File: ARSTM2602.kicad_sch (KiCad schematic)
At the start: 36 parts, among them J1 Conn_01x02_Socket, J11 Conn_01x02_Socket, J12 Conn_01x02_Socket, J13 Conn_01x02_Socket, J8 Conn_01x02_Socket, J9 Conn_ST_STDC14, SW2 SW_SPDT, SW3 SW_Push, SW5 SW_Wuerth_450301014042, SW6 SW_Wuerth_450301014042, U2 TCAN3414DRBR, U3 TCAN3414DRBR, U4 STM32H523CCTx, U5 BD33FC0FP

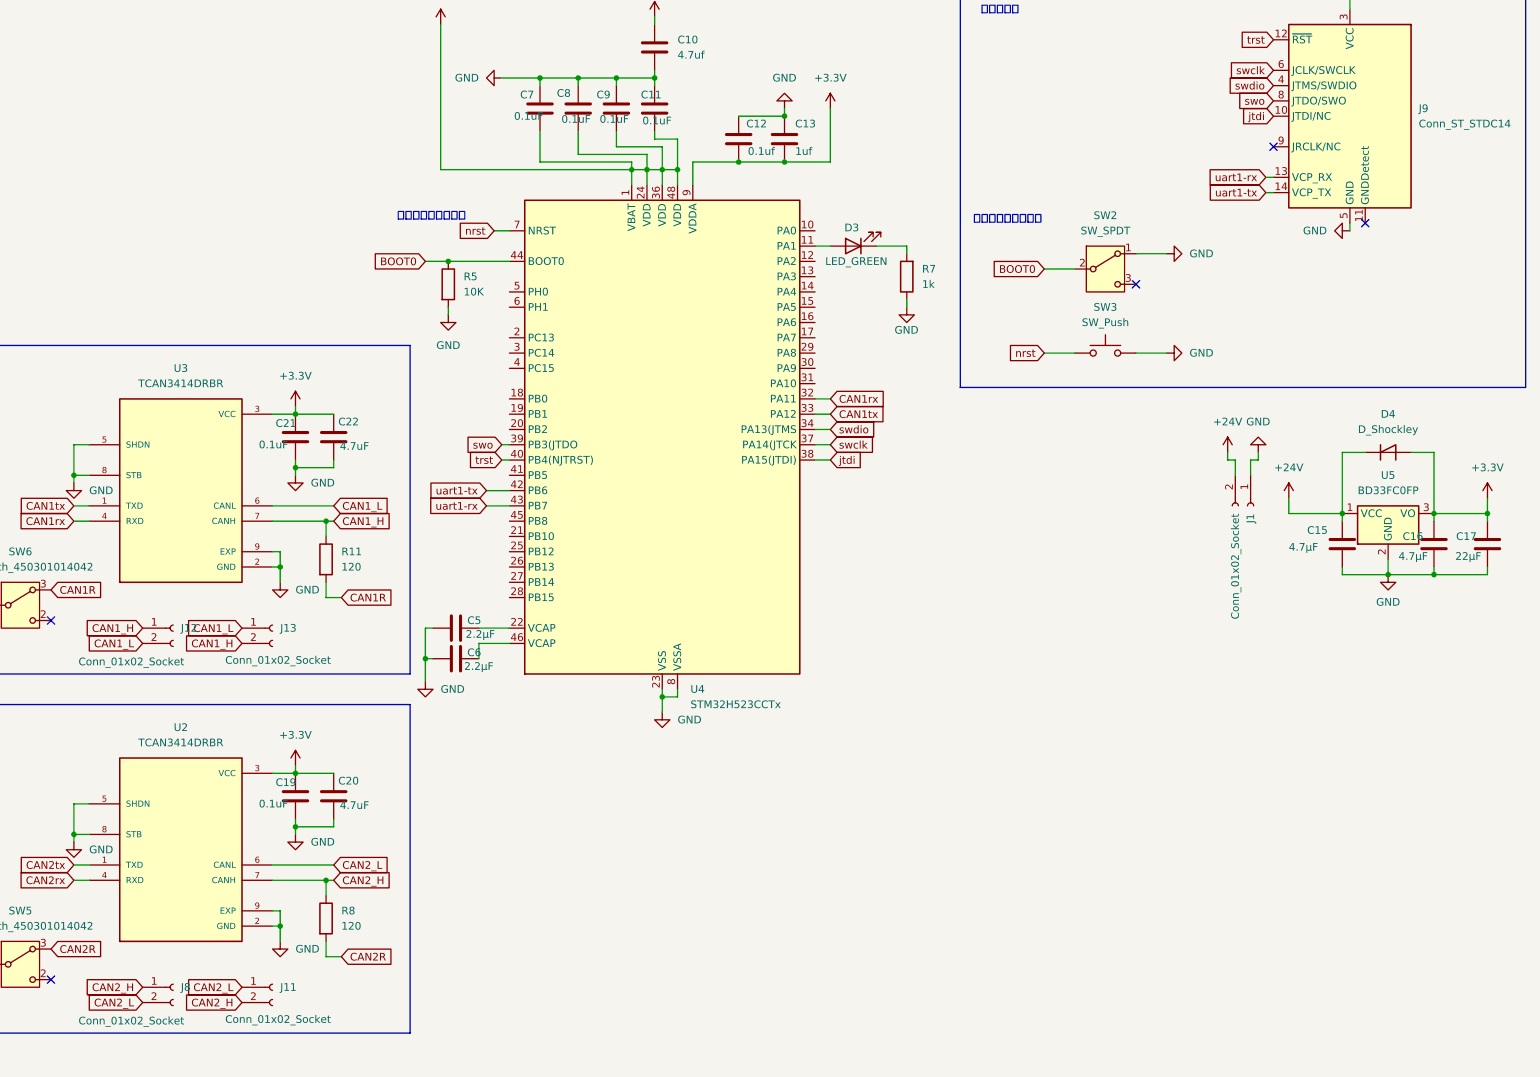
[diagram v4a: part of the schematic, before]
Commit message: サブマイコンx2を配置
ESPとラズパイを置いた
ラズパイはまだ途中
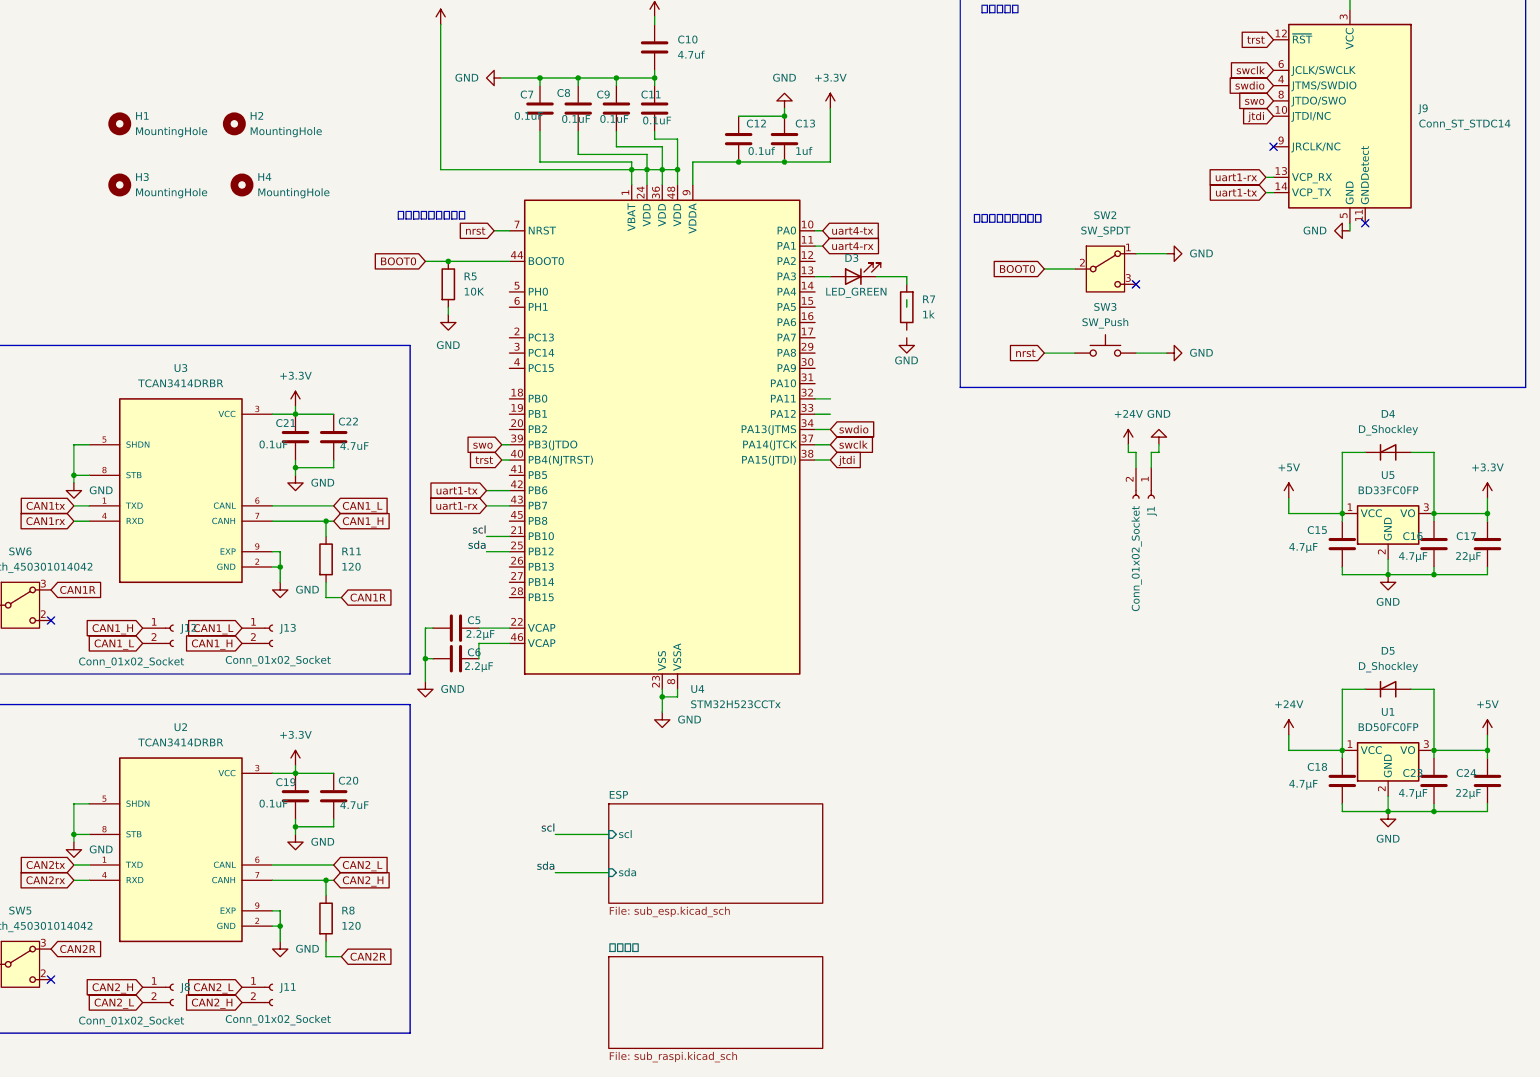
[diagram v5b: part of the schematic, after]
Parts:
- added C18, C23: 4.7μF, Capacitor_SMD:C_0805_2012Metric_Pad1.18x1.45mm_HandSolder, symbol Device:C
- added C24: 22μF, Capacitor_SMD:C_0805_2012Metric_Pad1.18x1.45mm_HandSolder, symbol Device:C
- added D5: D_Shockley, Diode_SMD:D_SOD-323_HandSoldering, symbol Device:D_Shockley
- added H1, H2, H3, H4: MountingHole, MountingHole:MountingHole_3.2mm_M3, symbol Mechanical:MountingHole
- added U1: BD50FC0FP, Package_TO_SOT_SMD:TO-252-2, symbol Regulator_Linear:BD50FC0FP
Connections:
- net +24V: now also C18.1, D5.1 (K), U1.1 (VCC); no longer C15.1, D4.1 (K), U5.1 (VCC)
- net CAN1rx: no longer U4.32 (PA11)
- net CAN1tx: no longer U4.33 (PA12)
- net GND: now also C18.2, C23.2, C24.2, U1.2 (GND); no longer R7.1
- net uart4-tx: now reaches U4.10 (PA0)
- net at D3.2 (A): now also U4.13 (PA3); no longer U4.11 (PA1)
- net scl: now reaches U4.21 (PB10)
- net sda: now reaches U4.25 (PB12)
- new net +5V: C15.1, C23.1, C24.1, D4.1 (K), D5.2 (A), U1.3 (VO), U5.1 (VCC)
- new net uart4-rx: U4.11 (PA1)
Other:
- added sheet ESP (sub_esp.kicad_sch)
- added sheet ラズパイ (sub_raspi.kicad_sch)
- moved on the sheet: J1

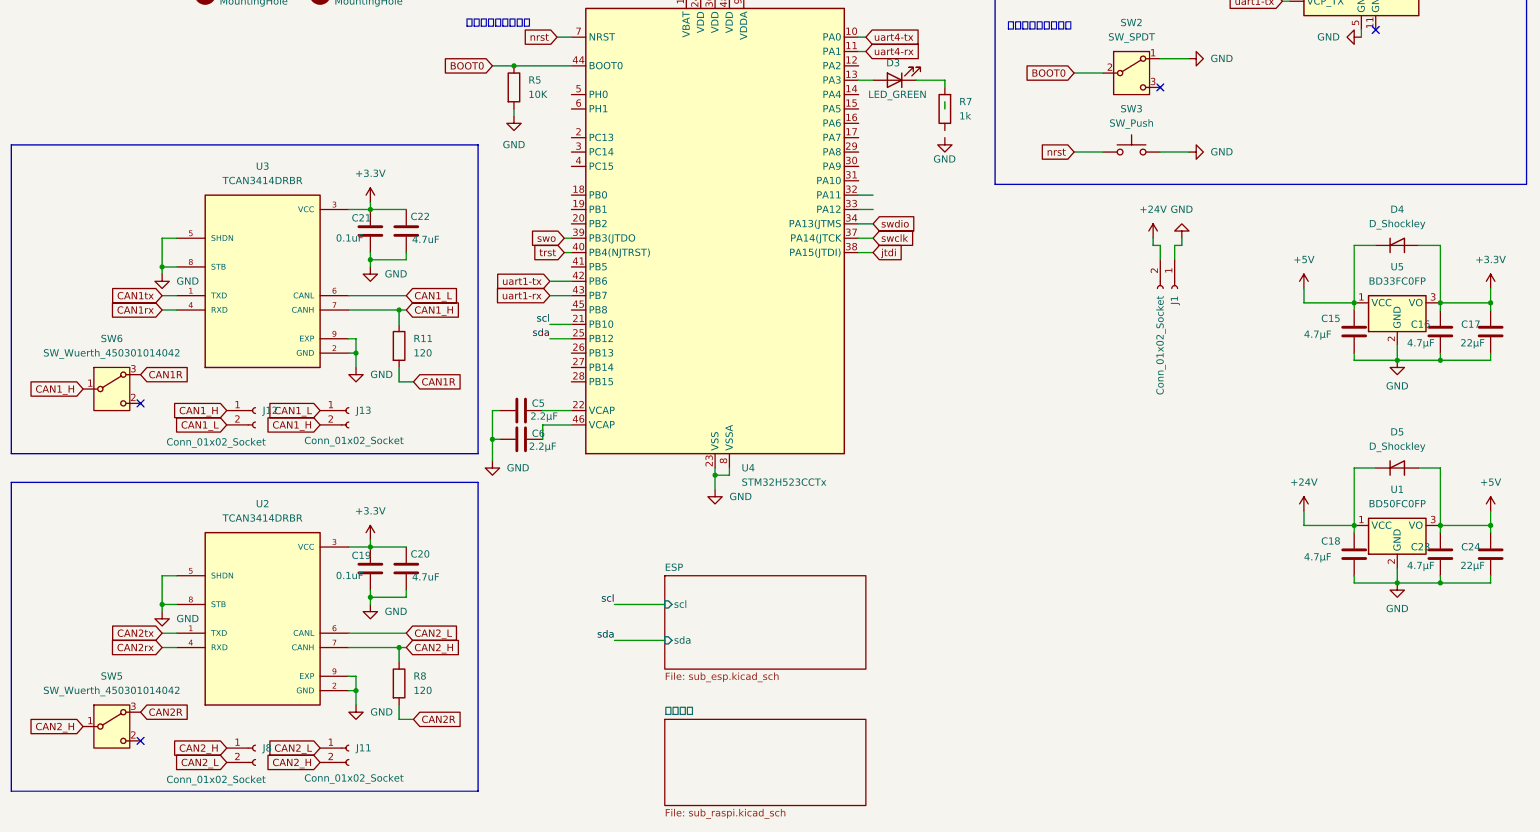
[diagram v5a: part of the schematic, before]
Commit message: 一部回路図変更と部品配置
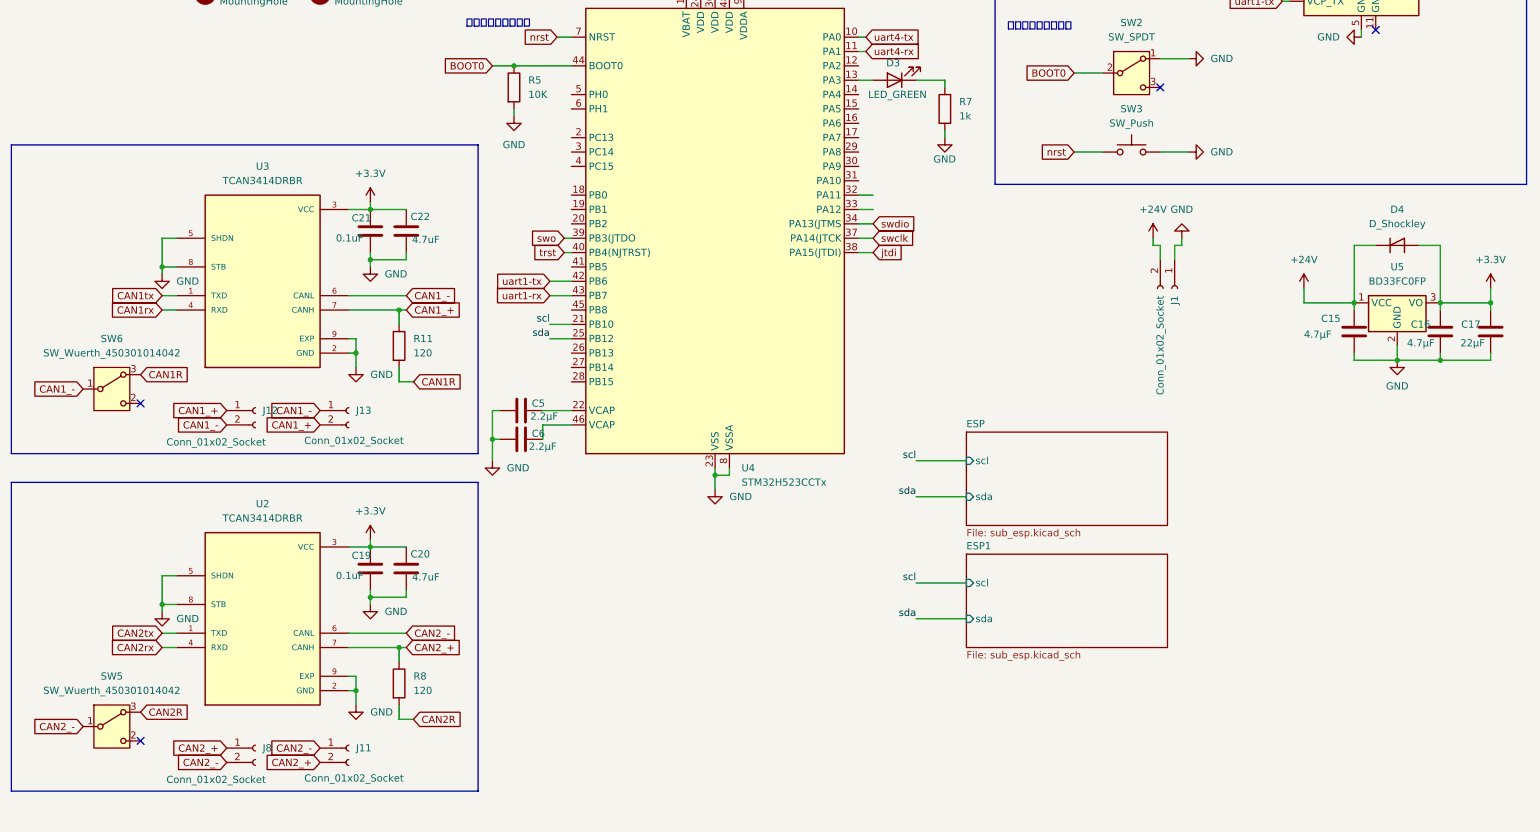
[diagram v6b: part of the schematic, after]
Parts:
- removed C18, C23: 4.7μF, Capacitor_SMD:C_0805_2012Metric_Pad1.18x1.45mm_HandSolder, symbol Device:C
- removed C24: 22μF, Capacitor_SMD:C_0805_2012Metric_Pad1.18x1.45mm_HandSolder, symbol Device:C
- removed D5: D_Shockley, Diode_SMD:D_SOD-323_HandSoldering, symbol Device:D_Shockley
- removed U1: BD50FC0FP, Package_TO_SOT_SMD:TO-252-2, symbol Regulator_Linear:BD50FC0FP
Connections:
- net +5V is gone; now on net +24V: C15.1, D4.1 (K), U5.1 (VCC)
- net GND: now also R7.1
- net CAN1_H renamed CAN1_+
- net CAN1_+: no longer SW6.1 (B)
- net CAN1_L renamed CAN1_-
- net CAN1_-: now also SW6.1 (B)
- net CAN2_H renamed CAN2_+
- net CAN2_+: no longer SW5.1 (B)
- net CAN2_L renamed CAN2_-
- net CAN2_-: now also SW5.1 (B)
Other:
- removed sheet ラズパイ
- added sheet ESP1 (sub_esp.kicad_sch)

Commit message: 電磁弁用回路の増設
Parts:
- removed SW5, SW6: SW_Wuerth_450301014042, Button_Switch_THT:SW_Slide-03_Wuerth-WS-SLTV_10x2.5x6.4_P2.54mm, symbol Switch:SW_Wuerth_450301014042
- added C14, C18, C23, C29, C32: 0.1uF, Capacitor_SMD:C_0603_1608Metric_Pad1.08x0.95mm_HandSolder, symbol Device:C
- added C24: 4.7uf, Capacitor_SMD:C_0805_2012Metric_Pad1.18x1.45mm_HandSolder, symbol Device:C
- added C30: 0.1uf, Capacitor_SMD:C_0603_1608Metric_Pad1.08x0.95mm_HandSolder, symbol Device:C
- added C31, C33: 1uf, Capacitor_SMD:C_0603_1608Metric_Pad1.08x0.95mm_HandSolder, symbol Device:C
- added D1, D2, D5: D, symbol Device:D
- added J10, J14, J15: Conn_01x02_Socket, Connector_JST:JST_XH_S2B-XH-A-1_1x02_P2.50mm_Horizontal, symbol Connector:Conn_01x02_Socket
- added J2: Conn_01x02_Socket, Connector_AMASS:AMASS_XT30PW-M_1x02_P2.50mm_Horizontal, symbol Connector:Conn_01x02_Socket
- added Q2, Q5, Q6: Q_NMOS_GSD, Package_TO_SOT_SMD:SOT-23_Handsoldering, symbol Transistor_FET:Q_NMOS_GSD
- added R15, R17, R19: 330, Resistor_SMD:R_0603_1608Metric_Pad0.98x0.95mm_HandSolder, symbol Device:R
- added R16, R18, R20, R21, R22, R23: 10k, Resistor_SMD:R_0603_1608Metric_Pad0.98x0.95mm_HandSolder, symbol Device:R_Small
- added SW10: SW_DPDT_x2, symbol Switch:SW_DPDT_x2
- added SW9: SW_DPDT_x2, Button_Switch_THT:SW_Slide-03_Wuerth-WS-SLTV_10x2.5x6.4_P2.54mm, symbol Switch:SW_DPDT_x2
- added U1: STM32G431RBTx, Package_QFP:LQFP-64_10x10mm_P0.5mm, symbol MCU_ST_STM32G4:STM32G431RBTx
- added U12, U8, U9: TLP785, Package_DIP:DIP-4_W7.62mm, symbol Isolator:TLP785
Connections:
- net +24V: now also D1.1 (K), D2.1 (K), D5.1 (K), J10.1 (Pin_1), J14.1 (Pin_1), J15.1 (Pin_1), J2.1 (Pin_1), U12.4, U8.4, U9.4
- net +3.3V: now also C14.1, C18.1, C23.1, C24.1, C29.1, C30.2, C31.2, C32.1, C33.2, U1.1 (VBAT), U1.16 (VDD), U1.28 (VREF+), U1.29 (VDDA), U1.32 (VDD), U1.48 (VDD), U1.64 (VDD)
- net CAN1R: now also SW10.1 (A)
- net CAN1_-: now also SW10.2 (B)
- net CAN1rx: now also U4.32 (PA11)
- net CAN1tx: now also U4.33 (PA12)
- net CAN2R: now also SW9.1 (A)
- net CAN2_-: now also SW9.2 (B)
- net CAN2rx: now also U4.25 (PB12)
- net CAN2tx: now also U4.26 (PB13)
- net GND: now also C14.2, C18.2, C23.2, C24.2, C29.2, C30.1, C31.1, C32.2, C33.1, U1.15 (VSS), U1.27 (VSSA), U1.31 (VSS), U1.47 (VSS), U1.63 (VSS), U12.2, U8.2, U9.2
- net scl: no longer U4.21 (PB10)
- net sda: no longer U4.25 (PB12)
- new net: D5.2 (A), J10.2 (Pin_2), Q2.3 (D)
- new net: R16.1, U8.3
- new net: Q2.1 (G), R16.2, R22.1
- new net: Q5.1 (G), R18.2, R21.1
- new net: D2.2 (A), J14.2 (Pin_2), Q5.3 (D)
- new net: R17.1, U9.1
- new net: R18.1, U9.3
- new net: D1.2 (A), J15.2 (Pin_2), Q6.3 (D)
- new net: R20.1, U12.3
- new net: Q6.1 (G), R20.2, R23.1
- new net: R15.1, U8.1
- new net: R19.1, U12.1
- new net GND1: J2.2 (Pin_2), Q2.2 (S), Q5.2 (S), Q6.2 (S), R21.2, R22.2, R23.2
- new net Si_1: R15.2
- new net Si_2: R17.2
- new net Si_3: R19.2
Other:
- moved on the sheet: C10, C11, C12, C13, C19, C20, C21, C22, C5, C6, C7, C8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

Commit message: 完成(電磁弁制御,モーター出力追加済み)
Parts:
- removed C10: 4.7uf, Capacitor_SMD:C_0805_2012Metric_Pad1.18x1.45mm_HandSolder, symbol Device:C
- removed C11, C19, C21, C7, C8, C9: 0.1uF, Capacitor_SMD:C_0603_1608Metric_Pad1.08x0.95mm_HandSolder, symbol Device:C
- removed C12: 0.1uf, Capacitor_SMD:C_0603_1608Metric_Pad1.08x0.95mm_HandSolder, symbol Device:C
- removed C13: 1uf, Capacitor_SMD:C_0603_1608Metric_Pad1.08x0.95mm_HandSolder, symbol Device:C
- removed C20, C22: 4.7uF, Capacitor_SMD:C_0603_1608Metric_Pad1.08x0.95mm_HandSolder, symbol Device:C
- removed C5, C6: 2.2μF, Capacitor_SMD:C_0603_1608Metric_Pad1.08x0.95mm_HandSolder, symbol Device:C
- removed D1, D2, D5: D, symbol Device:D
- removed D3: LED_GREEN, Capacitor_SMD:C_0603_1608Metric_Pad1.08x0.95mm_HandSolder, symbol Device:LED
- removed J10, J11, J12, J13, J14, J15, J8: Conn_01x02_Socket, Connector_JST:JST_XH_S2B-XH-A-1_1x02_P2.50mm_Horizontal, symbol Connector:Conn_01x02_Socket
- removed Q2, Q5, Q6: Q_NMOS_GSD, Package_TO_SOT_SMD:SOT-23_Handsoldering, symbol Transistor_FET:Q_NMOS_GSD
- removed R11, R8: 120, Resistor_SMD:R_0603_1608Metric_Pad0.98x0.95mm_HandSolder, symbol Device:R
- removed R15, R17, R19: 330, Resistor_SMD:R_0603_1608Metric_Pad0.98x0.95mm_HandSolder, symbol Device:R
- removed R16, R18, R20, R21, R22, R23: 10k, Resistor_SMD:R_0603_1608Metric_Pad0.98x0.95mm_HandSolder, symbol Device:R_Small
- removed R5: 10K, Resistor_SMD:R_0603_1608Metric_Pad0.98x0.95mm_HandSolder, symbol Device:R
- removed R7: 1k, Resistor_SMD:R_0603_1608Metric_Pad0.98x0.95mm_HandSolder, symbol Device:R
- removed SW10: SW_DPDT_x2, symbol Switch:SW_DPDT_x2
- removed SW2: SW_SPDT, Button_Switch_THT:SW_Slide-03_Wuerth-WS-SLTV_10x2.5x6.4_P2.54mm, symbol Switch:SW_SPDT
- removed SW9: SW_DPDT_x2, Button_Switch_THT:SW_Slide-03_Wuerth-WS-SLTV_10x2.5x6.4_P2.54mm, symbol Switch:SW_DPDT_x2
- removed U12, U8, U9: TLP785, Package_DIP:DIP-4_W7.62mm, symbol Isolator:TLP785
- removed U2, U3: TCAN3414DRBR, TCAN3414DRBR:XCVR_TCAN3414DRBR, symbol TCAN3414DRBR:TCAN3414DRBR
- removed U4: STM32H523CCTx, Package_QFP:LQFP-48_7x7mm_P0.5mm, symbol MCU_ST_STM32H5:STM32H523CCTx
- added J1, J2, J3, J4, J5, J6, J7: Conn_01x03_Pin, Connector_JST:JST_XH_S3B-XH-A-1_1x03_P2.50mm_Horizontal, symbol Connector:Conn_01x03_Pin
- SW2: renamed from SW3; footprint Button_Switch_THT:SW_PUSH_6mm -> Button_Switch_SMD:SW_Push_SPST_NO_Alps_SKRK
- renumbered C33 to C1, C15 to C10, C16 to C11, C17 to C12, C32 to C2, C14 to C3, C18 to C4, C23 to C5, C24 to C6, C29 to C7, C30 to C8, C31 to C9, D4 to D1, H3 to H2, H2 to H3, J9 to J10, J2 to J8, J1 to J9, U5 to U2
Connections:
- net uart1-rx is gone; now on net uart2-rx: J10.13 (VCP_RX)
- net uart1-tx is gone; now on net uart2-tx: J10.14 (VCP_TX)
- net +24V: now also J8.2 (Pin_2); no longer C10.1, D1.1 (K), J8.1 (Pin_1), J9.2 (Pin_2), U2.1 (VCC)
- net GND: now also J1.1 (Pin_1), J2.1 (Pin_1), J3.1 (Pin_1), J4.1 (Pin_1), J5.1 (Pin_1), J6.1 (Pin_1), J7.1 (Pin_1)
- net GND1: now also J8.1 (Pin_1); no longer J8.2 (Pin_2)
- net nrst: now also U1.7 (PG10)
- net swclk: now also U1.50 (PA14)
- net swdio: now also U1.49 (PA13)
- net Tim1ch3: now reaches U1.10 (PC2)
- net Tim1ch3: now also J2.2 (Pin_2)
- net dir2: now reaches U1.11 (PC3)
- net dir2: now also J2.3 (Pin_3)
- net Tim2ch1: now reaches U1.12 (PA0)
- net Tim2ch1: now also J3.2 (Pin_2)
- net dir3: now reaches U1.13 (PA1)
- net dir3: now also J3.3 (Pin_3)
- net Tim2ch3: now reaches U1.14 (PA2)
- net Tim2ch3: now also J4.2 (Pin_2)
- net dir4: now reaches U1.17 (PA3)
- net dir4: now also J4.3 (Pin_3)
- net Tim3ch2: now reaches U1.18 (PA4)
- net Tim3ch2: now also J5.2 (Pin_2)
- net dir5: now reaches U1.19 (PA5)
- net dir5: now also J5.3 (Pin_3)
- net Tim3ch1: now reaches U1.20 (PA6)
- net Tim3ch1: now also J6.2 (Pin_2)
- net dir6: now reaches U1.21 (PA7)
- net dir6: now also J6.3 (Pin_3)
- net Tim3ch3: now reaches U1.24 (PB0)
- net Tim3ch3: now also J7.2 (Pin_2)
- net dir7: now reaches U1.25 (PB1)
- net dir7: now also J7.3 (Pin_3)
- net spi_cs_2: now reaches U1.34 (PB12)
- net spi_sclk_2: now reaches U1.35 (PB13)
- net spi_miso_2: now reaches U1.36 (PB14)
- net spi_mosi_2: now reaches U1.37 (PB15)
- net spi_int_2: now reaches U1.38 (PC6)
- net spi_cs_3: now reaches U1.51 (PA15)
- net spi_sclk_3: now reaches U1.52 (PC10)
- net spi_miso_3: now reaches U1.53 (PC11)
- net spi_mosi_3: now reaches U1.54 (PC12)
- net spi_int_3: now reaches U1.55 (PD2)
- net uart2-rx: now reaches U1.57 (PB4)
- net uart2-tx: now reaches U1.58 (PB5)
- net can1_tx: now reaches U1.61 (PB8)
- net can1_rx: now reaches U1.62 (PB9)
- net Tim1ch1: now reaches U1.8 (PC0)
- net Tim1ch1: now also J1.2 (Pin_2)
- net dir1: now reaches U1.9 (PC1)
- net dir1: now also J1.3 (Pin_3)
- new net +7.5V: C10.1, D1.1 (K), J9.2 (Pin_2), U2.1 (VCC)
- no-connect marks 5 -> 2
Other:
- added sheet can1 (tcan.kicad_sch)
- added sheet solenoid_valve (solenoid_valve.kicad_sch)
- added sheet solenoid_valve1 (solenoid_valve.kicad_sch)
- added sheet solenoid_valve2 (solenoid_valve.kicad_sch)
- added sheet solenoid_valve3 (solenoid_valve.kicad_sch)
- added sheet solenoid_valve4 (solenoid_valve.kicad_sch)
- sheet ESP ports: added cs, int, miso, mosi, sclk; removed scl, sda
- sheet ESP1 ports: added cs, int, miso, mosi, sclk; removed scl, sda
- moved on the sheet: C1, C10, C11, C12, C2, C3, C4, C5, C6, C7, C8, C9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
